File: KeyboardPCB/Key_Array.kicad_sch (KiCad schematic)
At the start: 138 parts

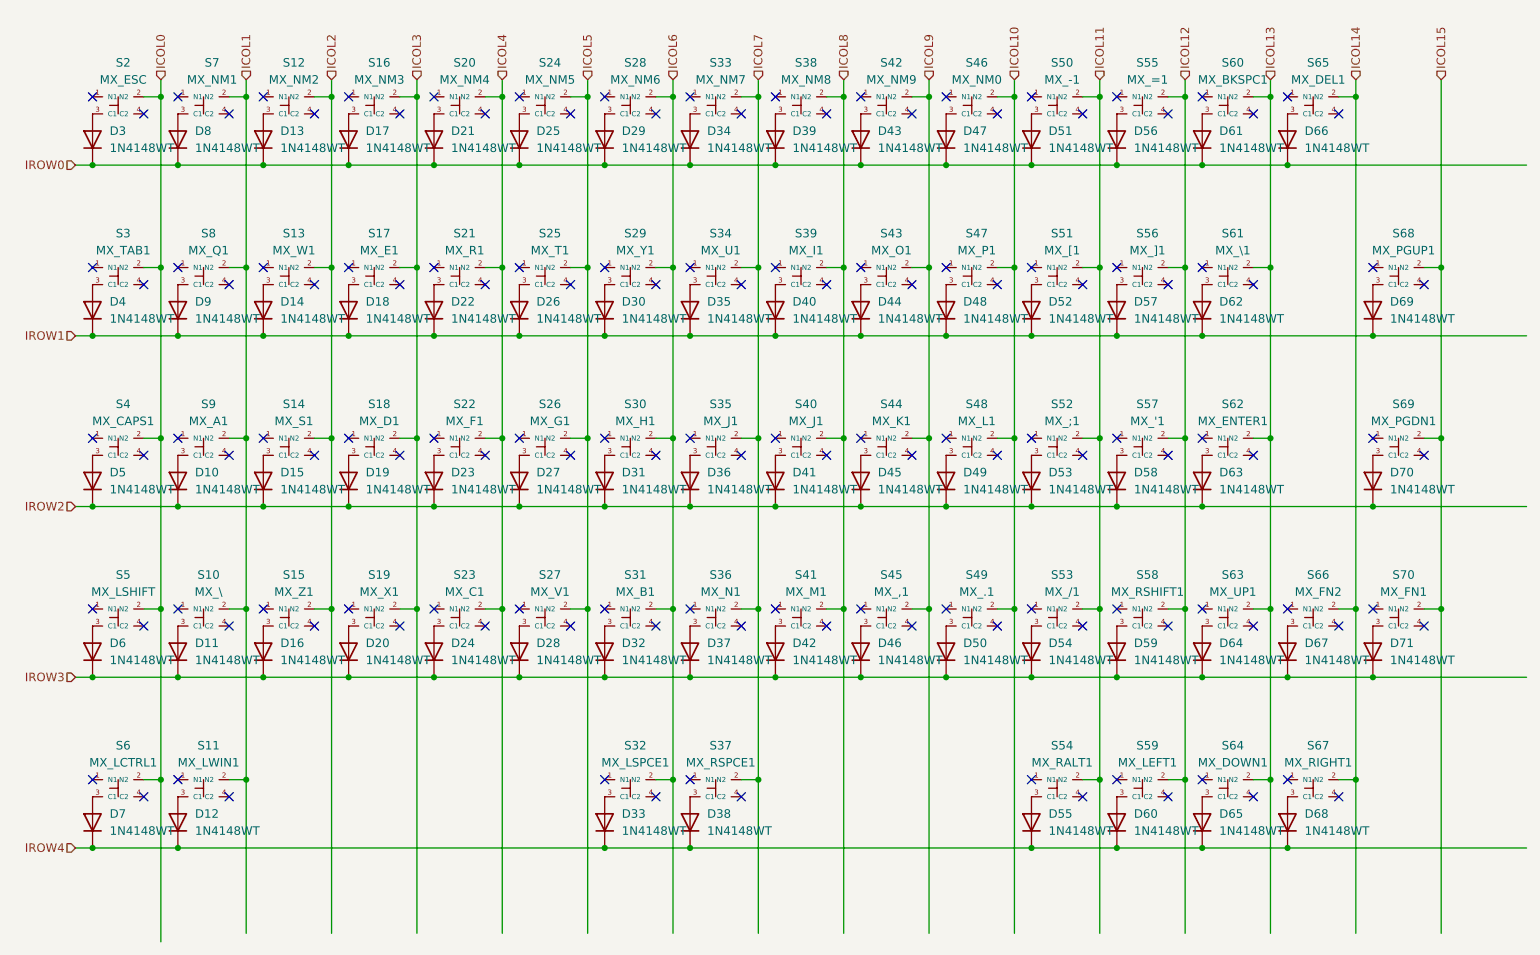
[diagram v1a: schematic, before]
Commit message: Reorganised key array
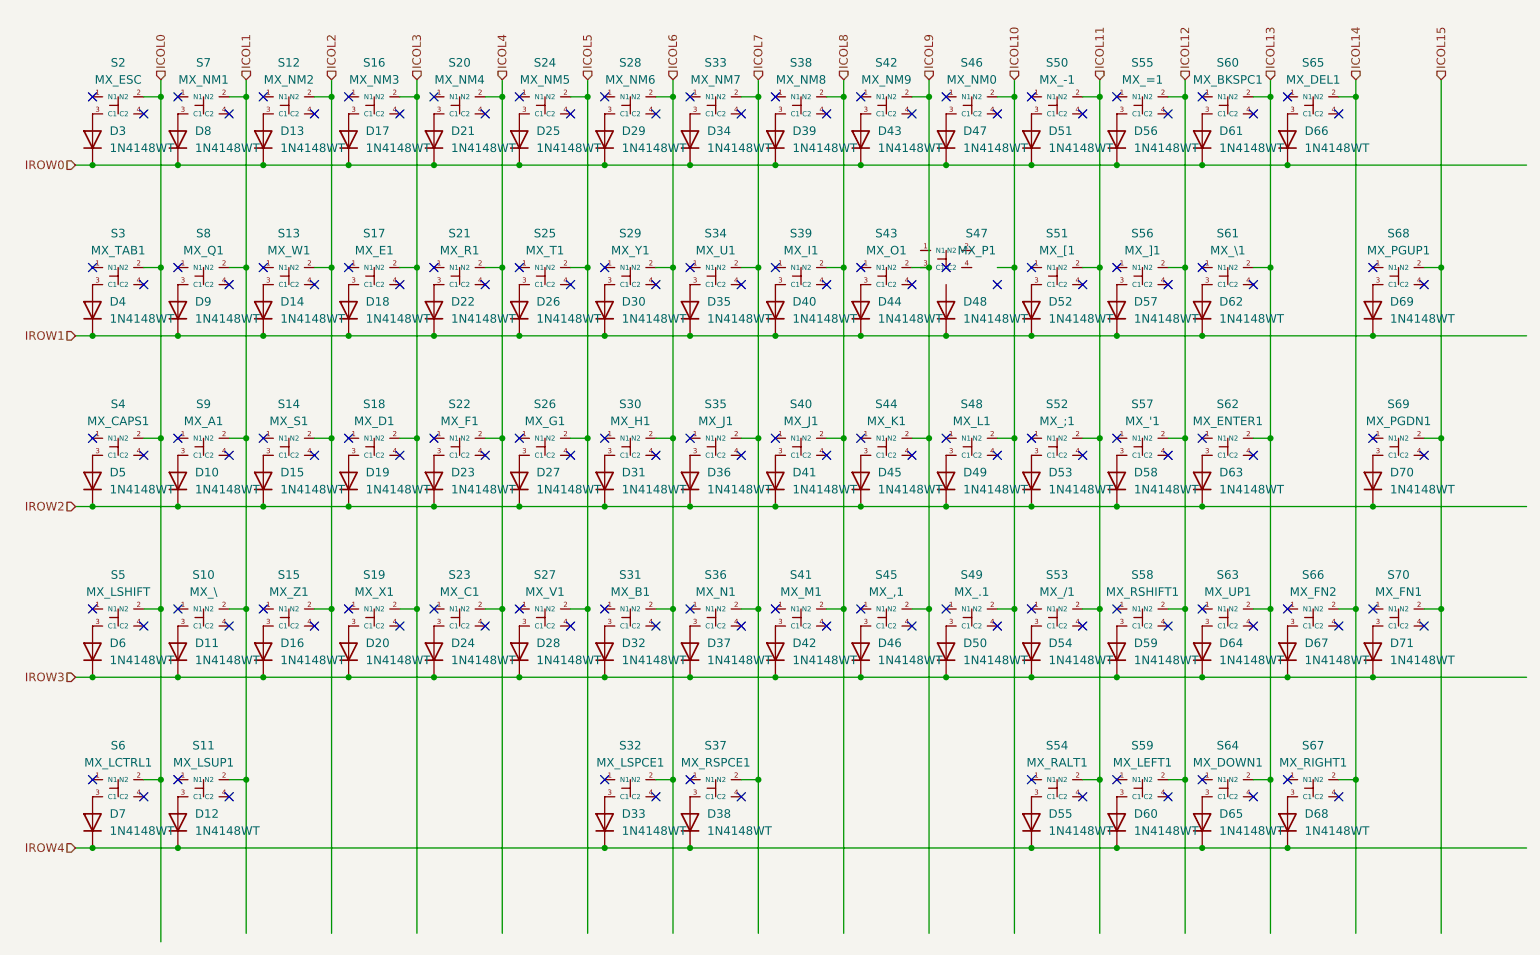
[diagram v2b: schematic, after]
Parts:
- S11: value MX_LWIN1 -> MX_LSUP1
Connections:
- net ICOL10: no longer S47.2 (N2)
- net at D48.2 (A): no longer S47.3 (C1)
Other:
- moved on the sheet: S47

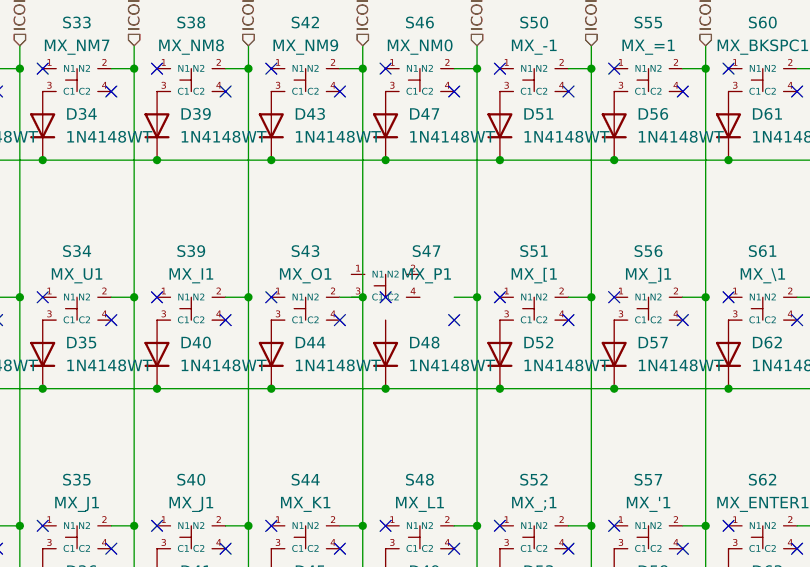
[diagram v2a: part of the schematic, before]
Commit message: Added some Capacitors
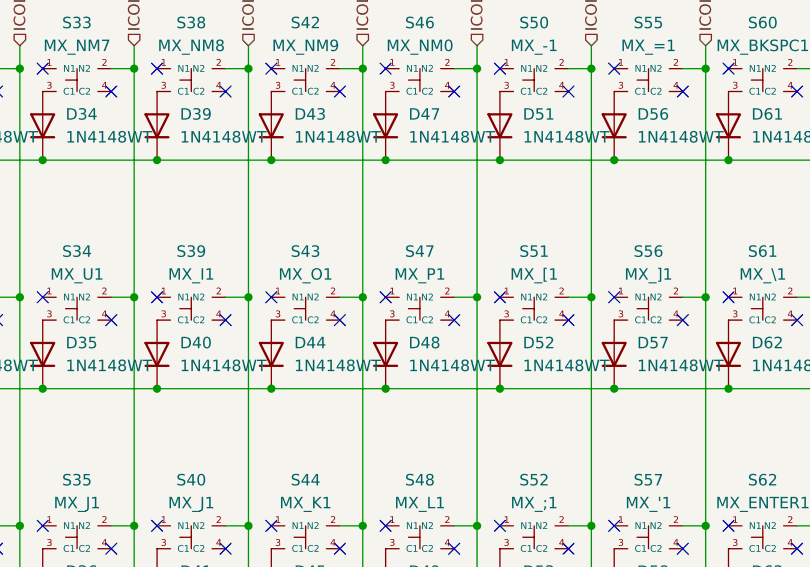
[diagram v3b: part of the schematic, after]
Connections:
- net ICOL10: now also S47.2 (N2)
- net at D48.2 (A): now also S47.3 (C1)
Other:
- moved on the sheet: S47
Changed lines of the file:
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@@
     )
   )
-  (symbol (lib_id "keyboard_syms:TS18-5-25-SL-160-SMT-TR") (at 154.94 52.07 0) (unit 1)
-    (in_bom yes) (on_board yes) (dnp no) (fields_autoplaced)
-    (property "Reference" "S47" (at 159.5 48.26 0)
+  (symbol (lib_id "keyboard_syms:TS18-5-25-SL-160-SMT-TR") (at 158.75 54.61 0) (unit 1)
+    (in_bom yes) (on_board yes) (dnp no)
+    (property "Reference" "S47" (at 158.75 48.26 0)
       (effects (font (size 1.27 1.27)))
     )
-    (property "Value" "MX_P1" (at 159.5 50.8 0)
+    (property "Value" "MX_P1" (at 158.75 50.8 0)
       (effects (font (size 1.27 1.27)))
     )
-    (property "Footprint" "TS18525SL160SMTTR" (at 182.88 49.53 0)
+    (property "Footprint" "TS18525SL160SMTTR" (at 186.69 52.07 0)
       (effects (font (size 1.27 1.27)) (justify left) hide)
     )
-    (property "Datasheet" "https://www.cuidevices.com/product/resource/ts18.pdf" (at 182.88 52.07 0)
+    (property "Datasheet" "https://www.cuidevices.com/product/resource/ts18.pdf" (at 186.69 54.61 0)
       (effects (font (size 1.27 1.27)) (justify left) hide)
     )
-    (property "Description" "Tactile Switches 5 x 5 mm, 2.5 mm Actuator Height, 160 gf, Silver, Surface Mount, TR, SPST, Tactile Switch" (at 182.88 54.61 0)
+    (property "Description" "Tactile Switches 5 x 5 mm, 2.5 mm Actuator Height, 160 gf, Silver, Surface Mount, TR, SPST, Tactile Switch" (at 186.69 57.15 0)
       (effects (font (size 1.27 1.27)) (justify left) hide)
     )
-    (property "Height" "2.6" (at 182.88 57.15 0)
+    (property "Height" "2.6" (at 186.69 59.69 0)
       (effects (font (size 1.27 1.27)) (justify left) hide)
     )
-    (property "Manufacturer_Name" "CUI Devices" (at 182.88 59.69 0)
+    (property "Manufacturer_Name" "CUI Devices" (at 186.69 62.23 0)
       (effects (font (size 1.27 1.27)) (justify left) hide)
     )
-    (property "Manufacturer_Part_Number" "TS18-5-25-SL-160-SMT-TR" (at 182.88 62.23 0)
+    (property "Manufacturer_Part_Number" "TS18-5-25-SL-160-SMT-TR" (at 186.69 64.77 0)
       (effects (font (size 1.27 1.27)) (justify left) hide)
     )
-    (property "Mouser Part Number" "179-TS18525SL160SMTT" (at 182.88 64.77 0)
+    (property "Mouser Part Number" "179-TS18525SL160SMTT" (at 186.69 67.31 0)
       (effects (font (size 1.27 1.27)) (justify left) hide)
     )
-    (property "Mouser Price/Stock" "https://www.mouser.co.uk/ProductDetail/CUI-Devices/TS18-5-25-SL-160-SMT-TR?qs=tlsG%2FOw5FFgGURAVArQGyg%3D%3D" (at 182.88 67.31 0)
+    (property "Mouser Price/Stock" "https://www.mouser.co.uk/ProductDetail/CUI-Devices/TS18-5-25-SL-160-SMT-TR?qs=tlsG%2FOw5FFgGURAVArQGyg%3D%3D" (at 186.69 69.85 0)
       (effects (font (size 1.27 1.27)) (justify left) hide)
     )
-    (property "Arrow Part Number" "" (at 181.61 69.85 0)
+    (property "Arrow Part Number" "" (at 185.42 72.39 0)
       (effects (font (size 1.27 1.27)) (justify left) hide)
     )
-    (property "Arrow Price/Stock" "" (at 181.61 72.39 0)
+    (property "Arrow Price/Stock" "" (at 185.42 74.93 0)
       (effects (font (size 1.27 1.27)) (justify left) hide)
     )
-    (property "Mouser Testing Part Number" "" (at 181.61 74.93 0)
+    (property "Mouser Testing Part Number" "" (at 185.42 77.47 0)
       (effects (font (size 1.27 1.27)) (justify left) hide)
     )
-    (property "Mouser Testing Price/Stock" "" (at 181.61 77.47 0)
+    (property "Mouser Testing Price/Stock" "" (at 185.42 80.01 0)
       (effects (font (size 1.27 1.27)) (justify left) hide)
     )

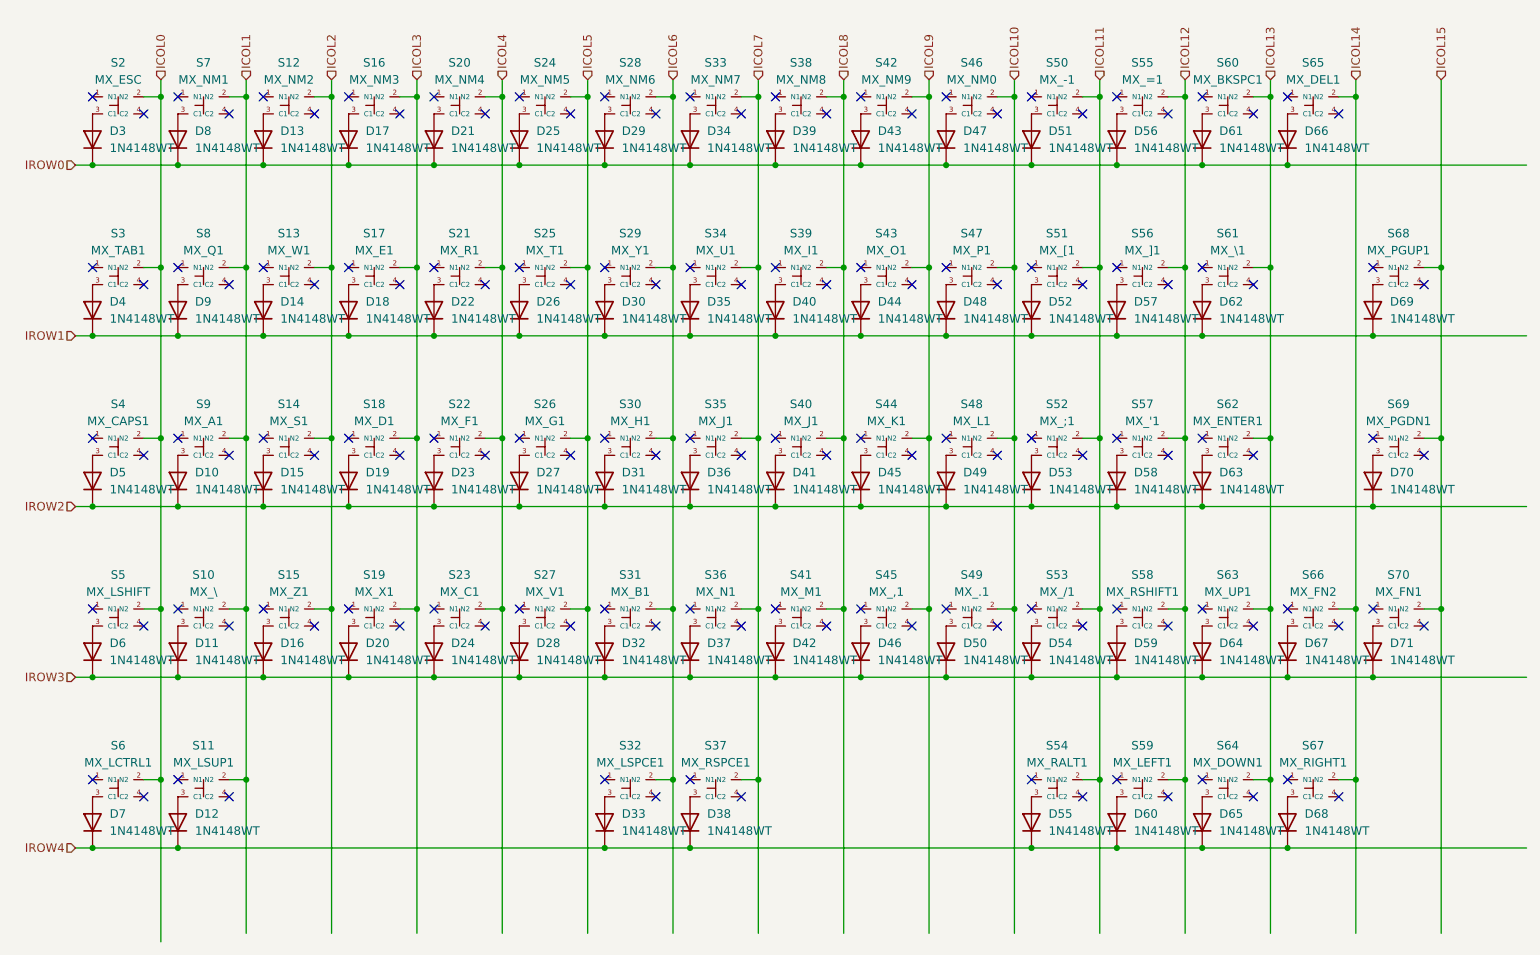
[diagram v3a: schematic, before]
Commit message: added footprints and changed symbols
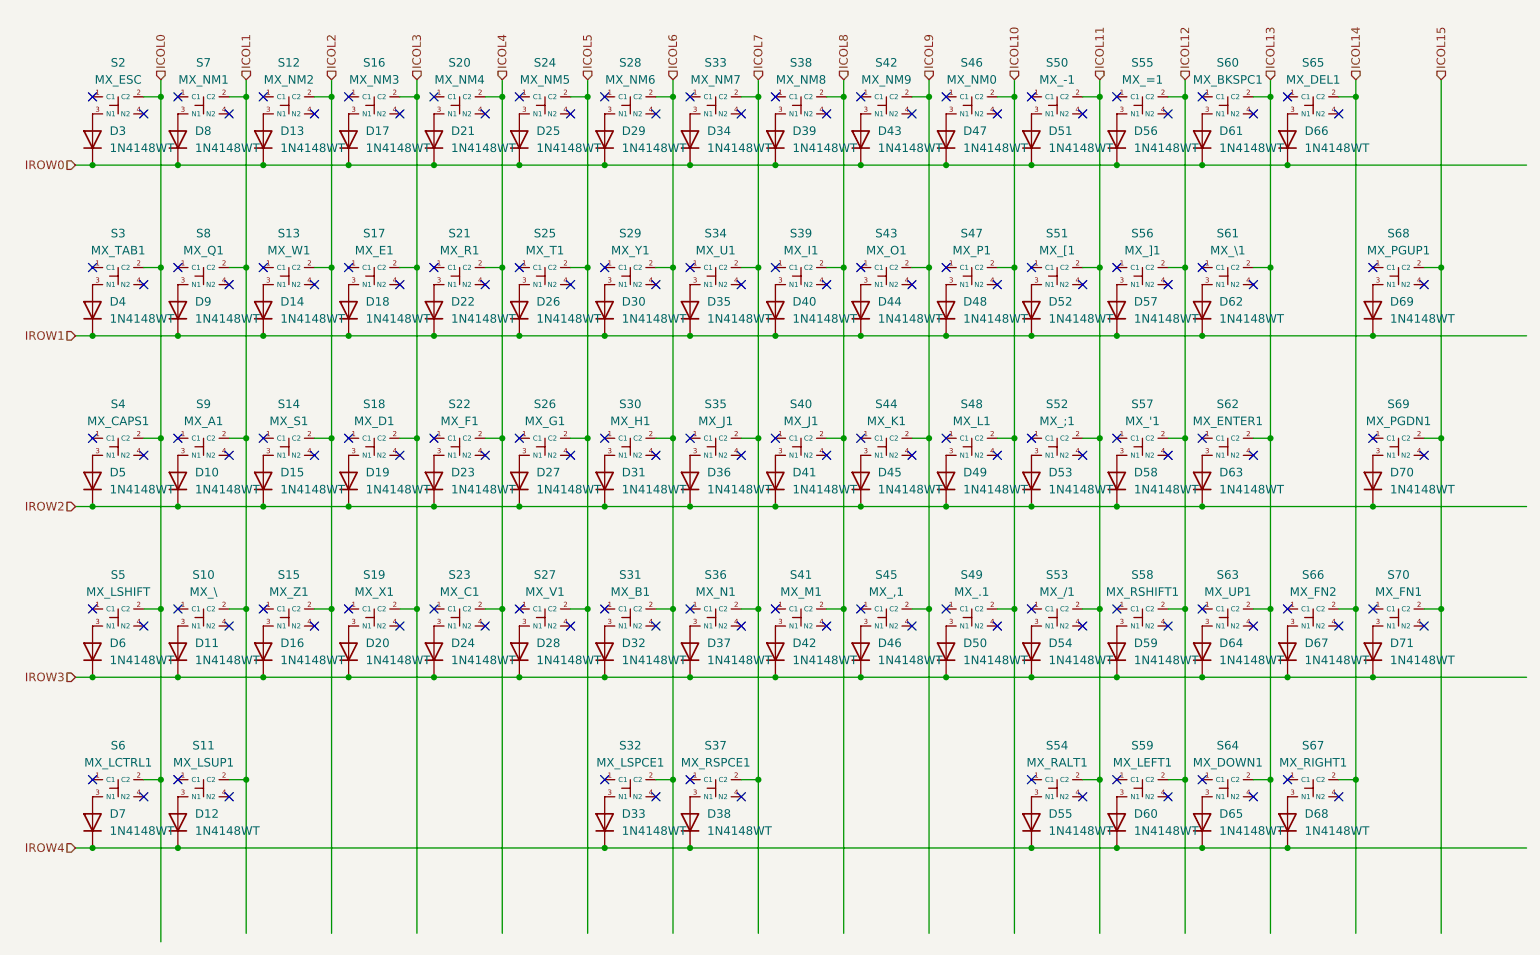
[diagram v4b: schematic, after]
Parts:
- S10, S11, S12, S13, S14, S15, S16, S17, S18, S19, S2, S20, S21, S22, S23, S24, S25, S26, S27, S28, S29, S3, S30, S31, S32, S33, S34, S35, S36, S37, S38, S39, S4, S40, S41, S42, S43, S44, S45, S46, S47, S48, S49, S5, S50, S51, S52, S53, S54, S55, S56, S57, S58, S59, S6, S60, S61, S62, S63, S64, S65, S66, S67, S68, S69, S7, S70, S8, S9: footprint TS18525SL160SMTTR -> keyboard_syms:B3FS1012P; symbol keyboard_syms:TS18-5-25-SL-160-SMT-TR -> keyboard_syms:B3FS-1012P; Arrow Part Number (none) -> B3FS-1012P; Arrow Price/Stock (none) -> https://www.arrow.com/en/products/b3fs-1012p/omron?region=n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; Height 2.6 -> 4.3; Manufacturer_Name CUI Devices -> Omron Electronics; Manufacturer_Part_Number TS18-5-25-SL-160-SMT-TR -> B3FS-1012P; Mouser Part Number 179-TS18525SL160SMTT -> 653-B3FS-1012P; Mouser Price/Stock https://www.mouser.co.uk/ProductDetail/CUI-Devices/TS18-5-2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 -> https://www.mouser.co.uk/ProductDetail/Omron-Electronics/B3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
